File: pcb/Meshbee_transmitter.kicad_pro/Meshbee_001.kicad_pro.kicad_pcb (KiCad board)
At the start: 2 copper layers, 42.5 x 164 mm, 26 parts, among them J1 sensor 0, J10 Battery, J11 ESP32, J2 sensor 1, J3 sensor 2, J4 sensor 3, J5 sensor 4, J6 sensor 5, J7 sensor 8, J8 sensor 9, J9 Reset_Button, SW1 button, SW2 reset, U1 Wemos_LoLin32_lite, U2 HT-RA62, U3 CD74HC4067M 16 channel multip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, U4 nice_nano

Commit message: - transferred some markings on the board to silkscreen layer - renumeration of WEMOS LOLIN32 LITE Pins - modified 3D-printed module for battery - created 3D-print module for MeshBee PCB
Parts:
- moved G*** 4.69 mm to (85.7, 116.8)
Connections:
- U1 pad 14: +3.3V -> /Notifier
- U1 pad 15: /S3 -> unconnected-(U1-Pad15)
- U1 pad 16: /S2 -> unconnected-(U1-2-Pad16)
- U1 pad 17: /S1 -> unconnected-(U1-0-Pad17)
- U1 pad 18: /S0 -> /data
- U1 pad 19: unconnected-(U1-5-Pad19) -> /TX
- U1 pad 21: /TX -> unconnected-(U1-5-Pad21)
- U1 pad 22: /data -> /S0
- U1 pad 23: unconnected-(U1-0-Pad23) -> /S1
- U1 pad 24: unconnected-(U1-2-Pad24) -> /S2
- U1 pad 25: unconnected-(U1-15-Pad25) -> /S3
- U1 pad 26: /Notifier -> +3.3V
- U3 pad 10: /S0 -> /S3
- U3 pad 11: /S1 -> /S2
- U3 pad 13: /S3 -> /S0
- U3 pad 14: /S2 -> /S1
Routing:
- net /Notifier: track 15.6 -> 47.7 mm
- net /S3: track 63.3 -> 80.4 mm
- net /S0: track 66.6 -> 80.8 mm
- net /S2: track 65.8 -> 79.9 mm
- net /S1: track 65.9 -> 79.9 mm
- net /TX: track 28.5 -> 37.9 mm
- net /data: track 85.2 -> 76.0 mm
- net +3.3V: track 273.3 -> 277.8 mm, vias 8 -> 9
- net Net-(U1-26): track 39.6 -> 37.6 mm
- net /RX: track 32.2 -> 31.3 mm
- net /HX711 CLK: track 150.0 -> 150.1 mm, vias 0 -> 2
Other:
- board text added: "MeshBee V1.0.1"
- board text removed: "MeshBee V1.0"

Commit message: - minor changes on silkscreen - added sensor circuit - added 3D-print designs for load cell holders
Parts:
- J9: value Reset_Button -> Reset/AP_Button
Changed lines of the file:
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@@
 	(title_block
 		(title "MeshBee")
-		(date "2026-07-11")
-		(rev "1.0")
+		(date "2026-08-09")
+		(rev "1.0.1")
 		(company "Fablab Imperia")
 	)
@@
 			)
 		)
-		(fp_text user "HX"
+		(fp_text user "W"
 			(at 8.75 -3.5 270)
 			(unlocked yes)
@@
 			)
 		)
-		(fp_text user "HX"
+		(fp_text user "W"
 			(at 8.75 -3.5 270)
 			(unlocked yes)
@@
 			)
 		)
-		(fp_text user "HX"
+		(fp_text user "W"
 			(at 8.75 -3.5 270)
 			(unlocked yes)
@@
 			)
 		)
-		(property "Value" "Reset_Button"
+		(property "Value" "Reset/AP_Button"
 			(at 1.25 4.6 90)
 			(layer "F.SilkS")
@@
 			)
 		)
-		(fp_text user "HX"
+		(fp_text user "W"
 			(at 8.75 -3.5 270)
 			(unlocked yes)
@@
 			)
 		)
-		(fp_text user "HX"
+		(fp_text user "W"
 			(at 8.75 -3.5 270)
 			(unlocked yes)
@@
 			)
 		)
-		(fp_text user "HX"
+		(fp_text user "W"
 			(at 8.75 -3.5 270)
 			(unlocked yes)
@@
 			)
 		)
-		(fp_text user "HX"
+		(fp_text user "W"
 			(at 8.75 -3.5 270)
 			(unlocked yes)
@@
 			)
 		)
-		(fp_text user "HX"
+		(fp_text user "W"
 			(at 8.75 -3.5 270)
 			(unlocked yes)
@@
 	)
 	(segment
-		(start 71.8 135.42)
-		(end 61.88 145.34)
+		(start 88.43 84.095)
+		(end 89.895 84.095)
 		(width 0.2)
 		(layer "B.Cu")
@@
 	)
 	(segment
-		(start 71.8 129.5)
-		(end 71.8 135.42)
+		(start 71.95 135.27)
+		(end 61.88 145.34)
 		(width 0.2)
 		(layer "B.Cu")
@@
 	)
 	(segment
-		(start 90.25 84.45)
-		(end 90.25 95.5)
-		(width 0.2)
-		(layer "B.Cu")
-		(net "/data")
-	)
-	(segment
-		(start 73.05 128.25)
-		(end 71.8 129.5)
-		(width 0.2)
-		(layer "B.Cu")
-		(net "/data")
-	)
-	(segment
-		(start 88.43 84.095)
-		(end 89.895 84.095)
+		(start 90.25 95.5)
+		(end 71.95 113.8)
 		(width 0.2)
 		(layer "B.Cu")
@@
 	)
 	(segment
-		(start 90.25 95.5)
-		(end 73.05 112.7)
+		(start 90.25 84.45)
+		(end 90.25 95.5)
 		(width 0.2)
 		(layer "B.Cu")
@@
 	)
 	(segment
-		(start 73.05 112.7)
-		(end 73.05 128.25)
+		(start 71.95 113.8)
+		(end 71.95 135.27)
 		(width 0.2)
 		(layer "B.Cu")

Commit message: - added possibility to measure battery voltage with the ESP32 to transmit to database
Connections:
- R3 pad 1: Net-(U4-D21/P0.31) -> Net-(U1-32)
- R4 pad 2: Net-(U4-D21/P0.31) -> Net-(U1-32)
- U1 pad 6: unconnected-(U1-32-Pad6) -> Net-(U1-32)
- U4 pad 21: Net-(U4-D21/P0.31) -> Net-(U1-32)
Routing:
- net Net-(U1-32): track 0.00 -> 64.8 mm, vias 0 -> 2
- net Net-(U4-D21/P0.31): track 34.9 -> 0.00 mm, vias 2 -> 0
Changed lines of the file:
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@@
 			(layers "*.Cu" "*.Mask")
 			(remove_unused_layers no)
-			(net "Net-(U4-D21{slash}P0.31)")
+			(net "Net-(U1-32)")
 			(pinfunction "D21/P0.31_21")
 			(pintype "input")
@@
 			(layers "F.Cu" "F.Mask" "F.Paste")
 			(roundrect_rratio 0.192308)
-			(net "Net-(U4-D21{slash}P0.31)")
+			(net "Net-(U1-32)")
 			(pintype "passive")
 		)
@@
 			(layers "*.Cu" "*.Mask")
 			(remove_unused_layers no)
-			(net "unconnected-(U1-32-Pad6)")
+			(net "Net-(U1-32)")
 			(pinfunction "32_6")
-			(pintype "bidirectional+no_connect")
+			(pintype "bidirectional")
 		)
 		(pad "7" thru_hole oval
@@
 			(layers "F.Cu" "F.Mask" "F.Paste")
 			(roundrect_rratio 0.192308)
-			(net "Net-(U4-D21{slash}P0.31)")
+			(net "Net-(U1-32)")
 			(pintype "passive")
 		)
@@
 	)
 	(segment
-		(start 62.5 48.5)
-		(end 62.2 48.2)
-		(width 0.2)
-		(layer "F.Cu")
-		(net "Net-(U4-D21{slash}P0.31)")
-	)
-	(segment
-		(start 62.2 48.8)
-		(end 62.5 48.5)
-		(width 0.2)
-		(layer "F.Cu")
-		(net "Net-(U4-D21{slash}P0.31)")
-	)
-	(segment
-		(start 62.2 48.2)
-		(end 62.2 46.6575)
-		(width 0.2)
-		(layer "F.Cu")
-		(net "Net-(U4-D21{slash}P0.31)")
-	)
-	(segment
-		(start 62.5 48.5)
-		(end 79.6 48.5)
-		(width 0.2)
-		(layer "F.Cu")
-		(net "Net-(U4-D21{slash}P0.31)")
-	)
-	(segment
-		(start 62.2 49.85)
-		(end 62.2 48.8)
-		(width 0.2)
-		(layer "F.Cu")
-		(net "Net-(U4-D21{slash}P0.31)")
-	)
-	(segment
-		(start 83.1 45)
-		(end 83.1 42.02)
-		(width 0.2)
-		(layer "F.Cu")
-		(net "Net-(U4-D21{slash}P0.31)")
-	)
-	(segment
-		(start 83.1 42.02)
-		(end 78.58 37.5)
-		(width 0.2)
-		(layer "F.Cu")
-		(net "Net-(U4-D21{slash}P0.31)")
-	)
-	(via
-		(at 79.6 48.5)
-		(size 0.6)
-		(drill 0.3)
-		(layers "F.Cu" "B.Cu")
-		(net "Net-(U4-D21{slash}P0.31)")
-	)
-	(via
-		(at 83.1 45)
-		(size 0.6)
-		(drill 0.3)
-		(layers "F.Cu" "B.Cu")
-		(net "Net-(U4-D21{slash}P0.31)")
-	)
-	(segment
-		(start 79.6 48.5)
-		(end 83.1 45)
-		(width 0.2)
-		(layer "B.Cu")
-		(net "Net-(U4-D21{slash}P0.31)")
-	)
-	(segment
 		(start 96 34.2)
 		(end 93.7 34.2)
@@
 		(net "Net-(J9-Pin_2)")
 	)
+	(segment
+		(start 65.35 48.5)
+		(end 65.65 48.8)
+		(width 0.2)
+		(layer "F.Cu")
+		(net "Net-(U1-32)")
+	)
+	(segment
+		(start 62.5 48.5)
+		(end 62.2 48.2)
+		(width 0.2)
+		(layer "F.Cu")
+		(net "Net-(U1-32)")
+	)
+	(segment
+		(start 62.2 48.8)
+		(end 62.5 48.5)
+		(width 0.2)
+		(layer "F.Cu")
+		(net "Net-(U1-32)")
+	)
+	(segment
+		(start 63.2 55)
+		(end 64.2 54)
+		(width 0.2)
+		(layer "F.Cu")
+		(net "Net-(U1-32)")
+	)
+	(segment
+		(start 64.2 51.45)
+		(end 65.65 50)
+		(width 0.2)
+		(layer "F.Cu")
+		(net "Net-(U1-32)")
+	)
+	(segment
+		(start 62.2 48.2)
+		(end 62.2 46.6575)
+		(width 0.2)
+		(layer "F.Cu")
+		(net "Net-(U1-32)")
+	)
+	(segment
+		(start 63.2 74.105)
+		(end 63.2 55)
+		(width 0.2)
+		(layer "F.Cu")
+		(net "Net-(U1-32)")
+	)
+	(segment
+		(start 65.65 48.8)
+		(end 65.95 48.5)
+		(width 0.2)
+		(layer "F.Cu")
+		(net "Net-(U1-32)")
+	)
+	(segment
+		(start 62.5 48.5)
+		(end 65.35 48.5)
+		(width 0.2)
+		(layer "F.Cu")
+		(net "Net-(U1-32)")
+	)
+	(segment
+		(start 64.2 54)
+		(end 64.2 51.45)
+		(width 0.2)
+		(layer "F.Cu")
+		(net "Net-(U1-32)")
+	)
+	(segment
+		(start 62.2 49.85)
+		(end 62.2 48.8)
+		(width 0.2)
+		(layer "F.Cu")
+		(net "Net-(U1-32)")
+	)
+	(segment
+		(start 65.65 50)
+		(end 65.65 48.8)
+		(width 0.2)
+		(layer "F.Cu")
+		(net "Net-(U1-32)")
+	)
+	(segment
+		(start 83.1 45)
+		(end 83.1 42.02)
+		(width 0.2)
+		(layer "F.Cu")
+		(net "Net-(U1-32)")
+	)
+	(segment
+		(start 83.1 42.02)
+		(end 78.58 37.5)
+		(width 0.2)
+		(layer "F.Cu")
+		(net "Net-(U1-32)")
+	)
+	(segment
+		(start 65.95 48.5)
+		(end 79.6 48.5)
+		(width 0.2)
+		(layer "F.Cu")
+		(net "Net-(U1-32)")
+	)
+	(segment
+		(start 65.57 76.475)
+		(end 63.2 74.105)
+		(width 0.2)
+		(layer "F.Cu")
+		(net "Net-(U1-32)")
+	)
+	(via
+		(at 79.6 48.5)
+		(size 0.6)
+		(drill 0.3)
+		(layers "F.Cu" "B.Cu")
+		(net "Net-(U1-32)")
+	)
+	(via
+		(at 83.1 45)
+		(size 0.6)
+		(drill 0.3)
+		(layers "F.Cu" "B.Cu")
+		(net "Net-(U1-32)")
+	)
+	(segment
+		(start 79.6 48.5)
+		(end 83.1 45)
+		(width 0.2)
+		(layer "B.Cu")
+		(net "Net-(U1-32)")
+	)
 	(zone

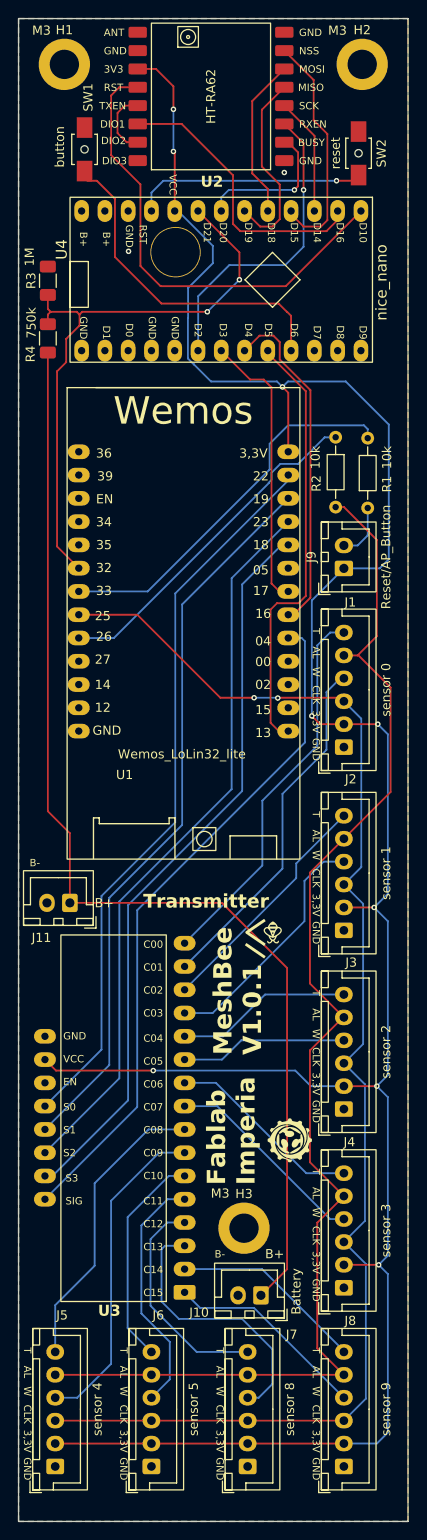
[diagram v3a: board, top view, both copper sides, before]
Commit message: - added capacitor on NRF52480 power lines, for possible crashes of nrf52840 during switch from solar panel to battery due to power glitches - changed GPIO of S3 pin of multiplexer to use GPIO22  for internal led as status indicator
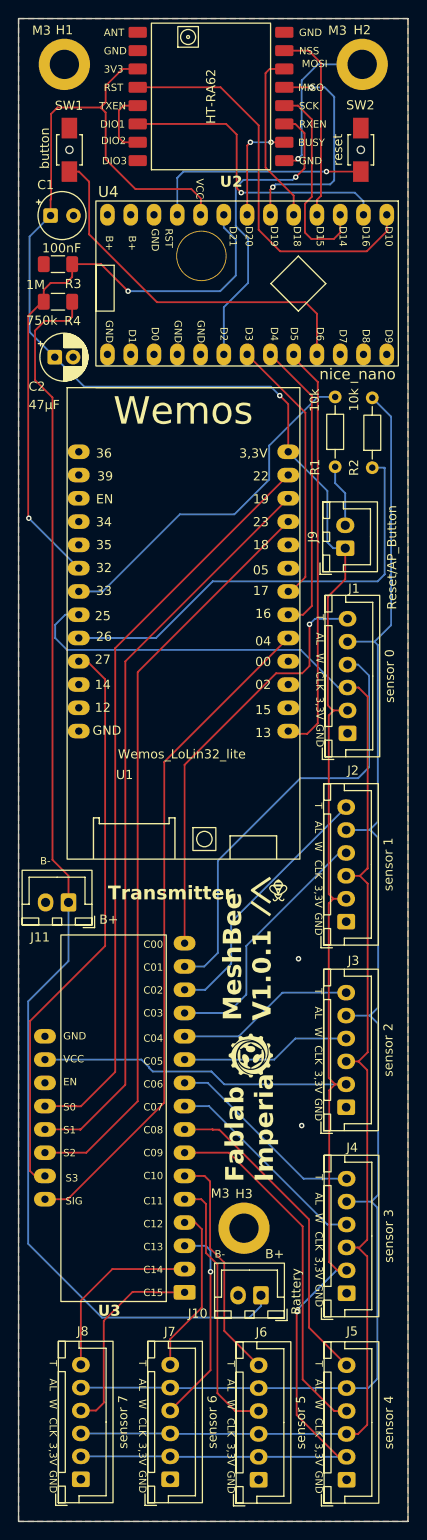
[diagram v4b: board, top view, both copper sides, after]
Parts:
- added C1: 100nF, Capacitor_THT:CP_Radial_Tantal_D5.0mm_P2.50mm, F.Cu at (62.5, 38.0)
- added C2: 47µF, Capacitor_THT:CP_Radial_D5.0mm_P2.00mm, F.Cu at (63.0, 53.5)
- J7: value sensor 8 -> sensor 6
- J8: value sensor 9 -> sensor 7
- moved J5 31.8 mm to (94.8, 175.9)
- moved J8 28.7 mm to (65.8, 175.9)
- moved J6 11.8 mm to (85.2, 175.9)
- moved G*** 10.2 mm to (84.3, 129.7)
- moved J7 8.57 mm to (75.5, 175.9)
- moved R1 5.73 mm to (93.5, 65.4)
- moved R2 5.20 mm to (97.6, 65.5), turned to 90 degrees
- moved G*** 4.64 mm to (86.3, 112.2)
- moved R4 4.15 mm to (63.3, 47.4), turned to 180 degrees
- moved U4 2.85 mm to (68.7, 53.1)
- moved J9 2.21 mm to (94.7, 74.3)
- moved R3 2.12 mm to (63.3, 43.3), turned to 180 degrees
- moved SW1 1.65 mm to (64.5, 30.8)
- moved J1 1.55 mm to (94.9, 94.5)
- moved J2 0.98 mm to (94.8, 115.0)
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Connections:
- U1 pad 10: unconnected-(U1-27-Pad10) -> /S3
- U1 pad 22: /S0 -> unconnected-(U1-18-Pad22)
- U1 pad 23: /S1 -> /S2
- U1 pad 24: /S2 -> /S1
- U1 pad 25: /S3 -> /S0
- U3 pad 10: /S3 -> /S0
- U3 pad 11: /S2 -> /S1
- U3 pad 13: /S0 -> /S3
- U3 pad 14: /S1 -> /S2
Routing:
- net /S3: track 80.4 -> 62.6 mm
- net GND: track 0.00 -> 17.6 mm, vias 2 -> 3
- net Net-(J10-Pin_1): track 124.6 -> 139.7 mm
- net Net-(U1-26): track 37.6 -> 49.2 mm
- net /alarm: track 143.2 -> 154.5 mm
- net Net-(U2-SCK): track 12.9 -> 22.7 mm
- net Net-(J1-Pin_4): track 38.9 -> 47.9 mm
- net /HX711 CLK: track 150.1 -> 158.9 mm, vias 2 -> 0
- net Net-(U2-RST): track 51.6 -> 44.0 mm
- net Net-(J7-Pin_4): track 29.8 -> 22.3 mm, vias 0 -> 1
- net +3.3V: track 277.8 -> 284.2 mm, vias 9 -> 2
- net Net-(J7-Pin_6): track 24.4 -> 18.4 mm
- net /TX: track 37.9 -> 32.3 mm
- net Net-(U4-D6/P1.00): track 35.9 -> 41.2 mm
- net Net-(J1-Pin_6): track 42.0 -> 46.5 mm, vias 0 -> 1
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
